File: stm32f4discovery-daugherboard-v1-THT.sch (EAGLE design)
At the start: 44 parts

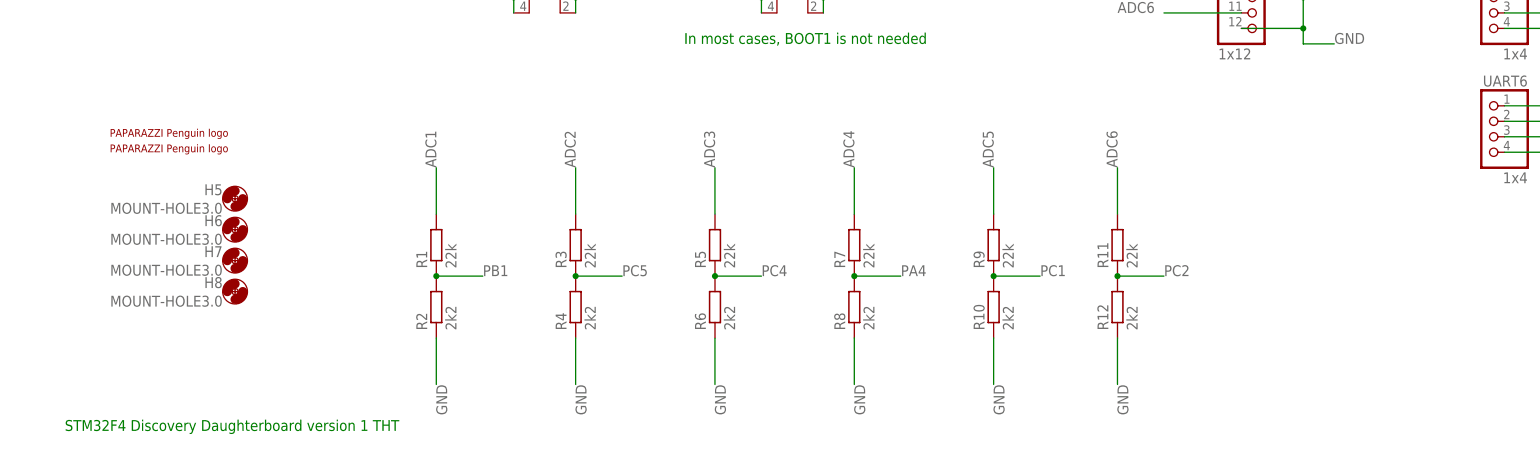
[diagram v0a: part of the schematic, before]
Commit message: all tht components, adc input protection with diodes
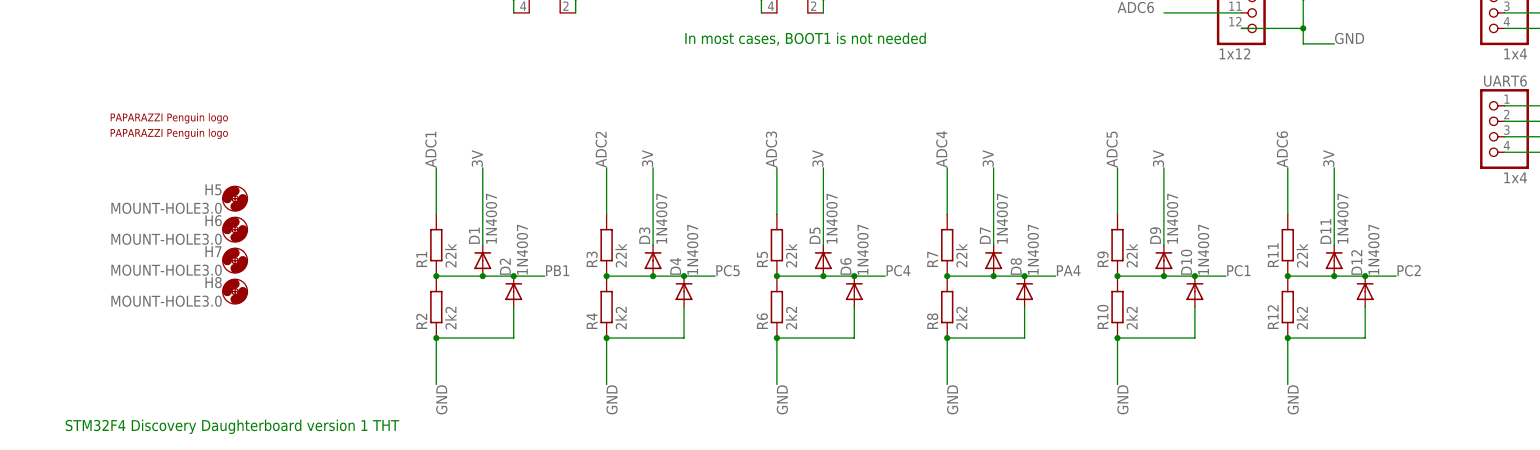
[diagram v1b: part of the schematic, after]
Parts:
- removed U$3: PAPARAZZI, paparazzi:PAPARAZZI
- added D1, D10, D11, D12, D2, D3, D4, D5, D6, D7, D8, D9: 1N4007, diode:1N4007
- added U$4: üAüARAZZI_1400, paparazzi:üAüARAZZI_1400
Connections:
- net 3V: now also D1.C, D11.C, D3.C, D5.C, D7.C, D9.C
- net GND: now also D10.A, D12.A, D2.A, D4.A, D6.A, D8.A
- net PA4: now also D7.A, D8.C
- net PB1: now also D1.A, D2.C
- net PC1: now also D10.C, D9.A
- net PC2: now also D11.A, D12.C
- net PC4: now also D5.A, D6.C
- net PC5: now also D3.A, D4.C
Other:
- moved on the sheet: R10, R11, R12, R3, R4, R5, R6, R7, R8, R9

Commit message: input protection
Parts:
- added D13: 1N4007, diode:1N4007
- added D14, D15: Z_DIODE_DO41-7.6, diode:Z_DIODE_DO41-7.6
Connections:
- removed net 5V: RIGHT.3, RIGHT.4
- net GND: now also D13.A, D14.A, D15.A
- net PWM_VIN: now also D13.C
- net VIN: now also D14.C, D15.C, RIGHT.3, RIGHT.4
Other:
- note added: "Z Dioded should have a z voltage at about 5.6V, 6V is the critical maximum voltage for some components"
- moved on the sheet: C1, C2
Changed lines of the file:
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@@
 <part name="D12" library="diode" deviceset="1N4007" device=""/>
 <part name="U$4" library="paparazzi" deviceset="üAüARAZZI_1400" device=""/>
+<part name="D13" library="diode" deviceset="1N4007" device=""/>
+<part name="D14" library="diode" deviceset="Z_DIODE_DO41-7.6" device=""/>
+<part name="D15" library="diode" deviceset="Z_DIODE_DO41-7.6" device=""/>
 </parts>
 <sheets>
@@
 <text x="-111.76" y="-83.82" size="1.778" layer="91">STM32F4 Discovery Daughterboard version 1 THT</text>
 <text x="-10.16" y="-20.32" size="1.778" layer="91">In most cases, BOOT1 is not needed</text>
+<text x="-111.76" y="-88.9" size="1.778" layer="91">Z Dioded should have a z voltage at about 5.6V, 6V is the critical maximum voltage for some  components</text>
 </plain>
 <instances>
@@
 <instance part="R11" gate="G$1" x="88.9" y="-53.34" rot="R90"/>
 <instance part="R12" gate="G$1" x="88.9" y="-63.5" rot="R90"/>
-<instance part="C1" gate="G$1" x="-101.6" y="45.72"/>
-<instance part="C2" gate="G$1" x="-93.98" y="45.72"/>
+<instance part="C1" gate="G$1" x="-106.68" y="45.72"/>
+<instance part="C2" gate="G$1" x="-99.06" y="45.72"/>
 <instance part="C3" gate="G$1" x="-101.6" y="71.12"/>
 <instance part="D1" gate="G$1" x="-43.18" y="-55.88" rot="R90"/>
@@
 <instance part="D12" gate="G$1" x="101.6" y="-60.96" rot="R90"/>
 <instance part="U$4" gate="G$1" x="-104.14" y="-33.02"/>
+<instance part="D13" gate="G$1" x="-88.9" y="68.58" rot="R90"/>
+<instance part="D14" gate="G$1" x="-91.44" y="43.18" rot="R90"/>
+<instance part="D15" gate="G$1" x="-81.28" y="43.18" rot="R90"/>
 </instances>
 <busses>
@@
 <segment>
 <pinref part="PWRDISCOVERY" gate="-2" pin="KL"/>
-<label x="-83.82" y="40.64" size="1.778" layer="95"/>
+<label x="-71.12" y="40.64" size="1.778" layer="95"/>
 <wire x1="-119.38" y1="40.64" x2="-109.22" y2="40.64" width="0.1524" layer="91"/>
 <pinref part="PWRDISCOVERY1" gate="-2" pin="KL"/>
-<wire x1="-109.22" y1="40.64" x2="-101.6" y2="40.64" width="0.1524" layer="91"/>
-<wire x1="-101.6" y1="40.64" x2="-93.98" y2="40.64" width="0.1524" layer="91"/>
-<wire x1="-93.98" y1="40.64" x2="-83.82" y2="40.64" width="0.1524" layer="91"/>
+<wire x1="-109.22" y1="40.64" x2="-106.68" y2="40.64" width="0.1524" layer="91"/>
+<wire x1="-106.68" y1="40.64" x2="-99.06" y2="40.64" width="0.1524" layer="91"/>
+<wire x1="-99.06" y1="40.64" x2="-91.44" y2="40.64" width="0.1524" layer="91"/>
+<wire x1="-91.44" y1="40.64" x2="-81.28" y2="40.64" width="0.1524" layer="91"/>
+<wire x1="-81.28" y1="40.64" x2="-71.12" y2="40.64" width="0.1524" layer="91"/>
 <wire x1="-119.38" y1="27.94" x2="-109.22" y2="27.94" width="0.1524" layer="91"/>
 <wire x1="-109.22" y1="27.94" x2="-109.22" y2="40.64" width="0.1524" layer="91"/>
 <junction x="-109.22" y="40.64"/>
 <pinref part="C1" gate="G$1" pin="-"/>
-<junction x="-101.6" y="40.64"/>
+<junction x="-106.68" y="40.64"/>
 <pinref part="C2" gate="G$1" pin="-"/>
-<junction x="-93.98" y="40.64"/>
+<junction x="-99.06" y="40.64"/>
+<pinref part="D14" gate="G$1" pin="A"/>
+<junction x="-91.44" y="40.64"/>
+<pinref part="D15" gate="G$1" pin="A"/>
+<junction x="-81.28" y="40.64"/>
 </segment>
 <segment>
@@
 <wire x1="-119.38" y1="66.04" x2="-101.6" y2="66.04" width="0.1524" layer="91"/>
 <pinref part="C3" gate="G$1" pin="-"/>
-<wire x1="-101.6" y1="66.04" x2="-76.2" y2="66.04" width="0.1524" layer="91"/>
+<wire x1="-101.6" y1="66.04" x2="-88.9" y2="66.04" width="0.1524" layer="91"/>
 <junction x="-101.6" y="66.04"/>
+<pinref part="D13" gate="G$1" pin="A"/>
+<wire x1="-88.9" y1="66.04" x2="-76.2" y2="66.04" width="0.1524" layer="91"/>
+<junction x="-88.9" y="66.04"/>
 </segment>
 <segment>
@@
 </segment>
 </net>
-<net name="5V" class="0">
-<segment>
-<wire x1="5.08" y1="68.58" x2="-2.54" y2="68.58" width="0.1524" layer="91"/>
-<label x="-2.54" y="68.58" size="1.778" layer="95" rot="R180"/>
-<pinref part="RIGHT" gate="A" pin="3"/>
-</segment>
-<segment>
-<wire x1="12.7" y1="68.58" x2="20.32" y2="68.58" width="0.1524" layer="91"/>
-<label x="20.32" y="68.58" size="1.778" layer="95"/>
-<pinref part="RIGHT" gate="A" pin="4"/>
-</segment>
-</net>
 <net name="3V" class="0">
 <segment>
@@
 <segment>
 <pinref part="PWRDISCOVERY" gate="-1" pin="KL"/>
-<label x="-83.82" y="48.26" size="1.778" layer="95"/>
+<label x="-71.12" y="48.26" size="1.778" layer="95"/>
 <wire x1="-119.38" y1="48.26" x2="-116.84" y2="48.26" width="0.1524" layer="91"/>
-<wire x1="-116.84" y1="48.26" x2="-101.6" y2="48.26" width="0.1524" layer="91"/>
+<wire x1="-116.84" y1="48.26" x2="-106.68" y2="48.26" width="0.1524" layer="91"/>
 <pinref part="PWRDISCOVERY1" gate="-1" pin="KL"/>
-<wire x1="-101.6" y1="48.26" x2="-93.98" y2="48.26" width="0.1524" layer="91"/>
-<wire x1="-93.98" y1="48.26" x2="-83.82" y2="48.26" width="0.1524" layer="91"/>
+<wire x1="-106.68" y1="48.26" x2="-99.06" y2="48.26" width="0.1524" layer="91"/>
+<wire x1="-99.06" y1="48.26" x2="-91.44" y2="48.26" width="0.1524" layer="91"/>
+<wire x1="-91.44" y1="48.26" x2="-81.28" y2="48.26" width="0.1524" layer="91"/>
+<wire x1="-81.28" y1="48.26" x2="-71.12" y2="48.26" width="0.1524" layer="91"/>
 <wire x1="-119.38" y1="33.02" x2="-116.84" y2="33.02" width="0.1524" layer="91"/>
 <wire x1="-116.84" y1="33.02" x2="-116.84" y2="48.26" width="0.1524" layer="91"/>
 <junction x="-116.84" y="48.26"/>
 <pinref part="C1" gate="G$1" pin="+"/>
-<junction x="-101.6" y="48.26"/>
+<junction x="-106.68" y="48.26"/>
 <pinref part="C2" gate="G$1" pin="+"/>
-<junction x="-93.98" y="48.26"/>
+<junction x="-99.06" y="48.26"/>
+<wire x1="-91.44" y1="45.72" x2="-91.44" y2="48.26" width="0.1524" layer="91"/>
+<junction x="-91.44" y="48.26"/>
+<pinref part="D14" gate="G$1" pin="C"/>
+<pinref part="D15" gate="G$1" pin="C"/>
+<wire x1="-81.28" y1="45.72" x2="-81.28" y2="48.26" width="0.1524" layer="91"/>
+<junction x="-81.28" y="48.26"/>
 </segment>
 <segment>
@@
 <junction x="-106.68" y="-2.54"/>
 </segment>
+<segment>
+<wire x1="5.08" y1="68.58" x2="-2.54" y2="68.58" width="0.1524" layer="91"/>
+<label x="-2.54" y="68.58" size="1.778" layer="95" rot="R180"/>
+<pinref part="RIGHT" gate="A" pin="3"/>
+</segment>
+<segment>
+<wire x1="12.7" y1="68.58" x2="20.32" y2="68.58" width="0.1524" layer="91"/>
+<label x="20.32" y="68.58" size="1.778" layer="95"/>
+<pinref part="RIGHT" gate="A" pin="4"/>
+</segment>
 </net>
 <net name="ADC2" class="0">
@@
 <wire x1="-119.38" y1="73.66" x2="-101.6" y2="73.66" width="0.1524" layer="91"/>
 <pinref part="C3" gate="G$1" pin="+"/>
-<wire x1="-101.6" y1="73.66" x2="-76.2" y2="73.66" width="0.1524" layer="91"/>
+<wire x1="-101.6" y1="73.66" x2="-88.9" y2="73.66" width="0.1524" layer="91"/>
 <junction x="-101.6" y="73.66"/>
-</segment>
-<segment>
+<pinref part="D13" gate="G$1" pin="C"/>
+<wire x1="-88.9" y1="73.66" x2="-76.2" y2="73.66" width="0.1524" layer="91"/>
+<wire x1="-88.9" y1="71.12" x2="-88.9" y2="73.66" width="0.1524" layer="91"/>
+<junction x="-88.9" y="73.66"/>
+</segment>
+<segment>

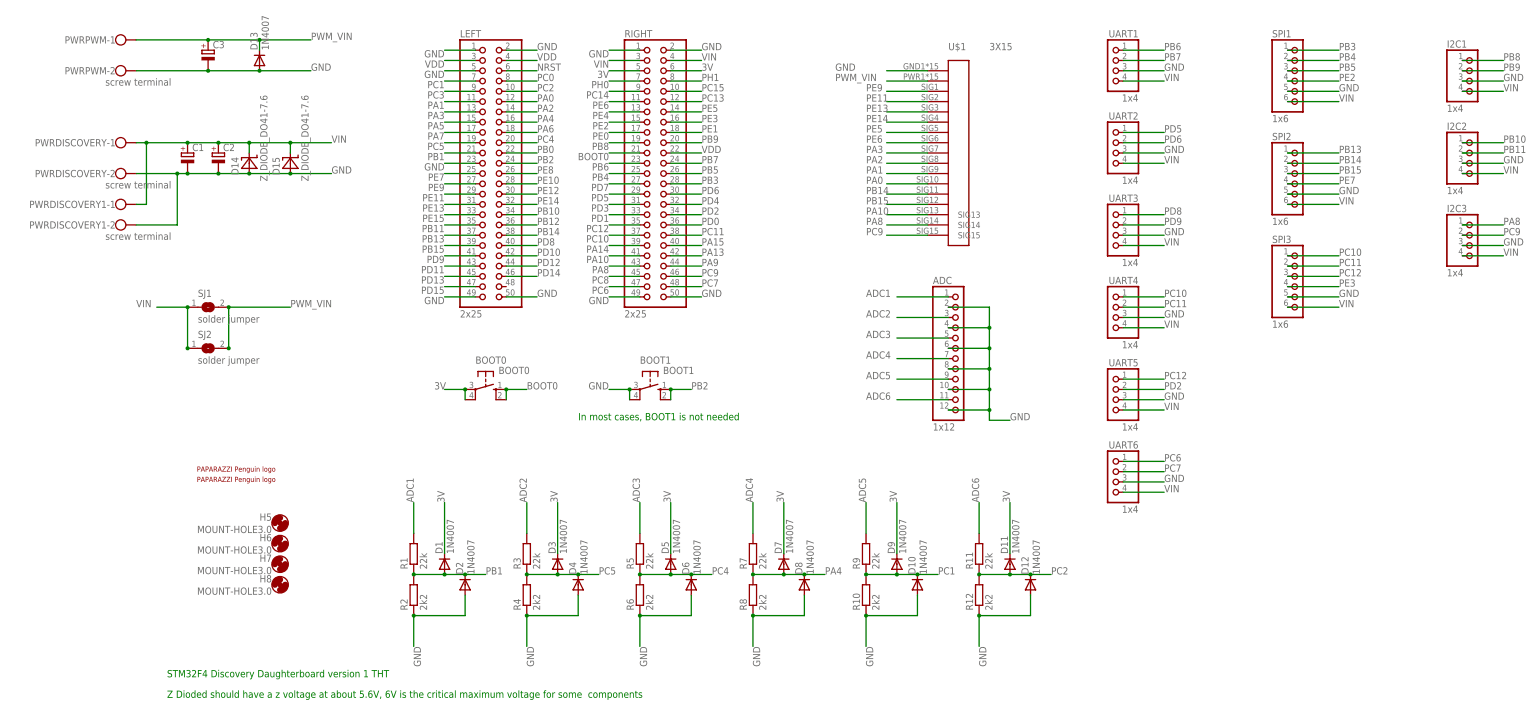
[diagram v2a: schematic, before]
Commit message: deleted old version, small changes in tht version
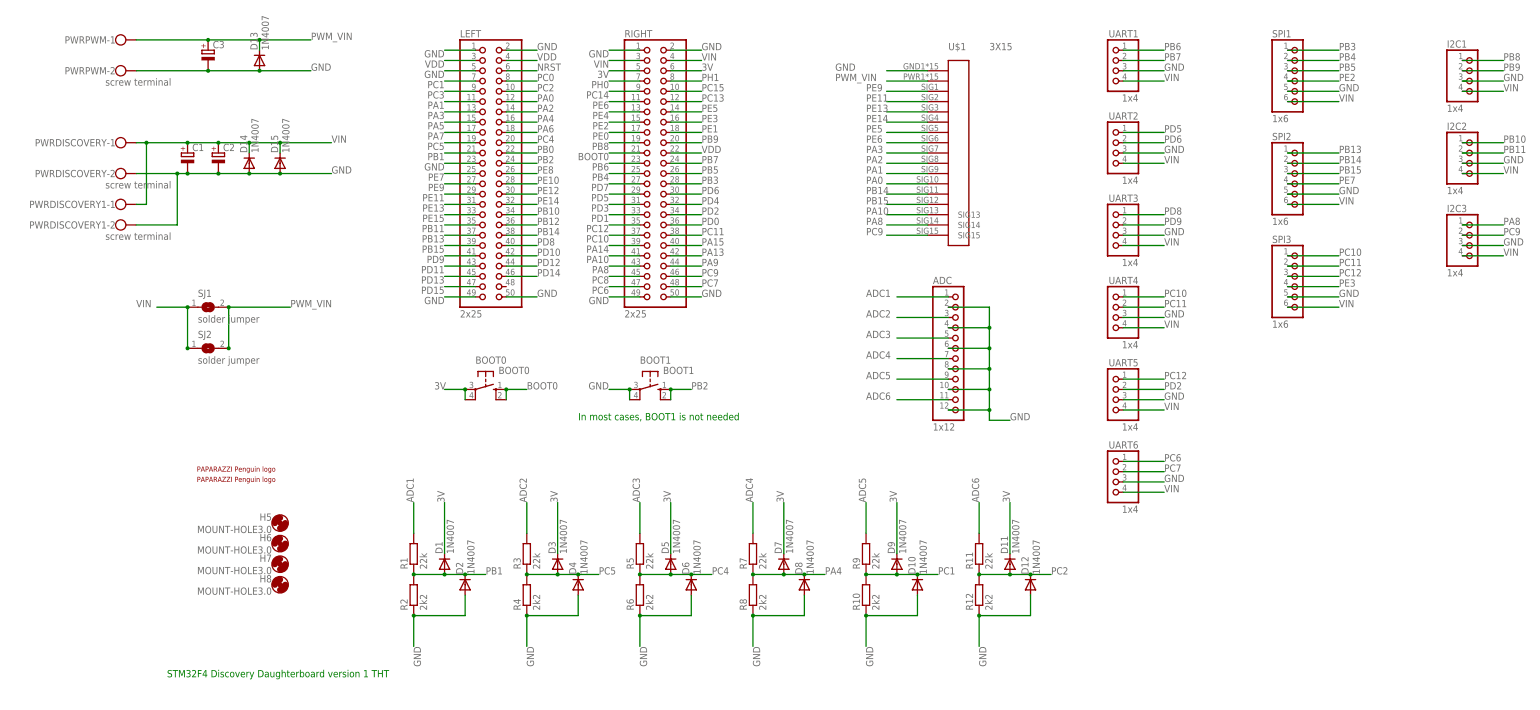
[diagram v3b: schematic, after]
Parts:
- D14, D15: value Z_DIODE_DO41-7.6 -> 1N4007; device diode:Z_DIODE_DO41-7.6 -> diode:1N4007
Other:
- note removed: "Z Dioded should have a z voltage at about 5.6V, 6V is the critical maximum voltage for some components"
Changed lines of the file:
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@@
 <part name="U$4" library="paparazzi" deviceset="üAüARAZZI_1400" device=""/>
 <part name="D13" library="diode" deviceset="1N4007" device=""/>
-<part name="D14" library="diode" deviceset="Z_DIODE_DO41-7.6" device=""/>
-<part name="D15" library="diode" deviceset="Z_DIODE_DO41-7.6" device=""/>
+<part name="D14" library="diode" deviceset="1N4007" device=""/>
+<part name="D15" library="diode" deviceset="1N4007" device=""/>
 </parts>
 <sheets>
@@
 <text x="-111.76" y="-83.82" size="1.778" layer="91">STM32F4 Discovery Daughterboard version 1 THT</text>
 <text x="-10.16" y="-20.32" size="1.778" layer="91">In most cases, BOOT1 is not needed</text>
-<text x="-111.76" y="-88.9" size="1.778" layer="91">Z Dioded should have a z voltage at about 5.6V, 6V is the critical maximum voltage for some  components</text>
 </plain>
 <instances>
@@
 <instance part="D13" gate="G$1" x="-88.9" y="68.58" rot="R90"/>
 <instance part="D14" gate="G$1" x="-91.44" y="43.18" rot="R90"/>
-<instance part="D15" gate="G$1" x="-81.28" y="43.18" rot="R90"/>
+<instance part="D15" gate="G$1" x="-83.82" y="43.18" rot="R90"/>
 </instances>
 <busses>
@@
 <wire x1="-106.68" y1="40.64" x2="-99.06" y2="40.64" width="0.1524" layer="91"/>
 <wire x1="-99.06" y1="40.64" x2="-91.44" y2="40.64" width="0.1524" layer="91"/>
-<wire x1="-91.44" y1="40.64" x2="-81.28" y2="40.64" width="0.1524" layer="91"/>
-<wire x1="-81.28" y1="40.64" x2="-71.12" y2="40.64" width="0.1524" layer="91"/>
+<wire x1="-91.44" y1="40.64" x2="-83.82" y2="40.64" width="0.1524" layer="91"/>
+<wire x1="-83.82" y1="40.64" x2="-71.12" y2="40.64" width="0.1524" layer="91"/>
 <wire x1="-119.38" y1="27.94" x2="-109.22" y2="27.94" width="0.1524" layer="91"/>
 <wire x1="-109.22" y1="27.94" x2="-109.22" y2="40.64" width="0.1524" layer="91"/>
@@
 <junction x="-91.44" y="40.64"/>
 <pinref part="D15" gate="G$1" pin="A"/>
-<junction x="-81.28" y="40.64"/>
+<junction x="-83.82" y="40.64"/>
 </segment>
 <segment>
@@
 <wire x1="-106.68" y1="48.26" x2="-99.06" y2="48.26" width="0.1524" layer="91"/>
 <wire x1="-99.06" y1="48.26" x2="-91.44" y2="48.26" width="0.1524" layer="91"/>
-<wire x1="-91.44" y1="48.26" x2="-81.28" y2="48.26" width="0.1524" layer="91"/>
-<wire x1="-81.28" y1="48.26" x2="-71.12" y2="48.26" width="0.1524" layer="91"/>
+<wire x1="-91.44" y1="48.26" x2="-83.82" y2="48.26" width="0.1524" layer="91"/>
+<wire x1="-83.82" y1="48.26" x2="-71.12" y2="48.26" width="0.1524" layer="91"/>
 <wire x1="-119.38" y1="33.02" x2="-116.84" y2="33.02" width="0.1524" layer="91"/>
 <wire x1="-116.84" y1="33.02" x2="-116.84" y2="48.26" width="0.1524" layer="91"/>
@@
 <pinref part="D14" gate="G$1" pin="C"/>
 <pinref part="D15" gate="G$1" pin="C"/>
-<wire x1="-81.28" y1="45.72" x2="-81.28" y2="48.26" width="0.1524" layer="91"/>
-<junction x="-81.28" y="48.26"/>
-</segment>
-<segment>
+<wire x1="-83.82" y1="45.72" x2="-83.82" y2="48.26" width="0.1524" layer="91"/>
+<junction x="-83.82" y="48.26"/>
+</segment>
+<segment>
